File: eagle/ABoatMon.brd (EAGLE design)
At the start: 86.4 x 61 mm, 30 parts, among them J1 5V, J2 GND, J3 GND, J4 5V, X1 MKDSN1,5/2-5,08

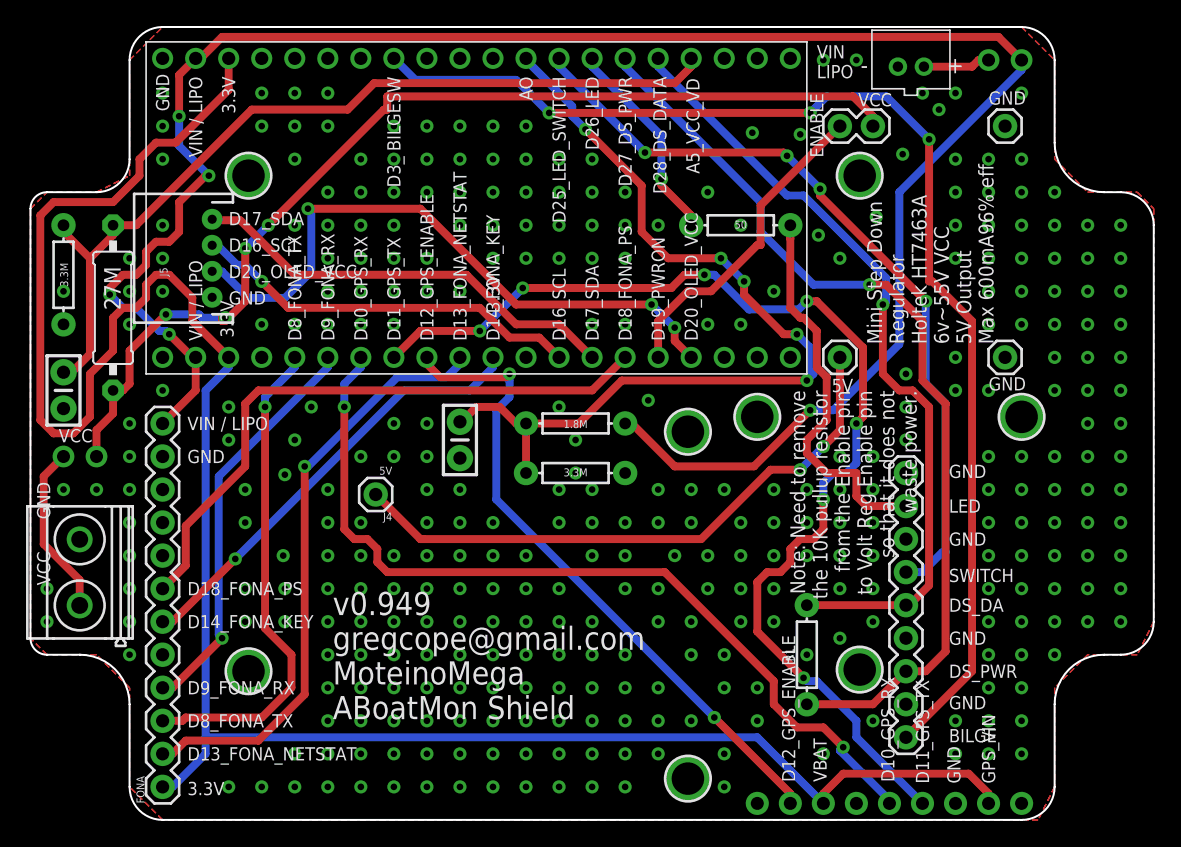
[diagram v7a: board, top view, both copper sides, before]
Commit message: v0.959 board layout, moved to 0.1 not jst
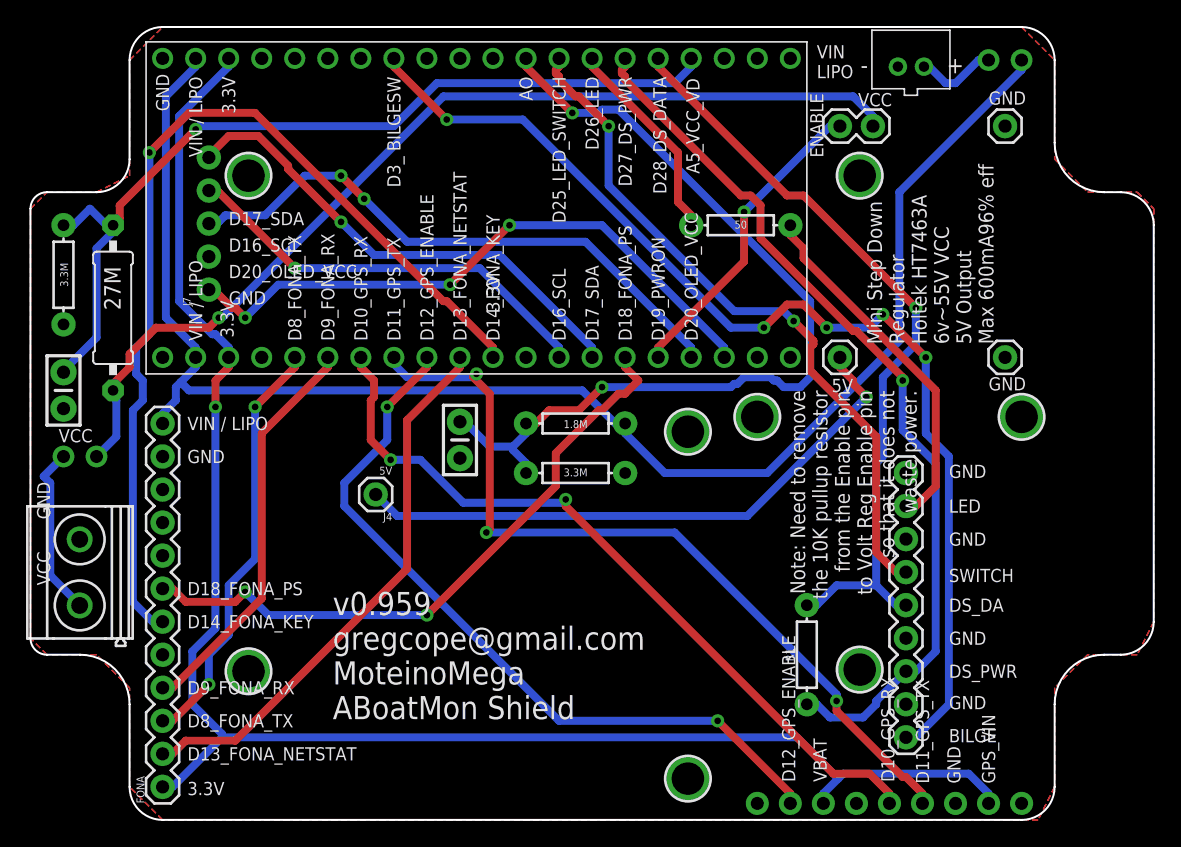
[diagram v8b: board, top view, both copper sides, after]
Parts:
- removed J5: (no value), SparkFun-Connectors:JST-4-PTH
- added J7: (no value), SparkFun-Connectors:1X05_NO_SILK
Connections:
- new net D21_SPARE: J7.1, MOTEINO_MEGA.D21
- net D16_SCL: now also J7.4; no longer J5.3
- net D17_SDA: now also J7.5; no longer J5.4
- net D20_OLED_VCC: now also J7.3; no longer J5.2
- net GND: now also J7.2; no longer J5.1
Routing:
- net D21_SPARE: track 0.00 -> 48.2 mm, vias 0 -> 3
- net D14_FONA_KEY: track 34.3 -> 74.3 mm
- net 3.3V: track 165.7 -> 127.9 mm, vias 0 -> 1
- net VIN: track 155.9 -> 120.2 mm, vias 5 -> 0
- net D11_GPS_TX: track 87.5 -> 63.7 mm, vias 7 -> 3
- net D3_BILGESW: track 94.4 -> 84.9 mm, vias 3 -> 5
- net D12_GPS_ENABLE: track 50.4 -> 58.3 mm
- net D10_GPS_RX: track 66.7 -> 59.3 mm
- net D25_LED_SWITCH: track 60.2 -> 53.8 mm, vias 4 -> 2
- net D8_FONA_TX: track 38.1 -> 32.6 mm, vias 1 -> 2
- net VCC_JUMPER: track 80.3 -> 75.9 mm, vias 4 -> 1
- net D20_OLED_VCC: track 49.2 -> 44.9 mm, vias 3 -> 2
- net D17_SDA: track 33.7 -> 37.9 mm, vias 0 -> 1
- net D13_FONA_NETSTAT: track 46.0 -> 42.6 mm, vias 1 -> 0
- net D27_DS_PWR: track 71.4 -> 68.9 mm
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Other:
- board text added: "v0.959 gregcope@gmail.com MoteinoMega ABoatMon Shield"
- board text removed: "v0.949 gregcope@gmail.com MoteinoMega ABoatMon Shield"
